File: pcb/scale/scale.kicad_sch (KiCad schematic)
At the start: 86 parts, among them J1 USB_C_Receptacle_USB2.0, J2 Conn_01x07, J3 Conn_01x04, SW1 SW_Push, SW10 SW_Push, SW11 SW_Push, SW12 SW_Push, SW13 SW_Push, SW14 SW_Push, SW15 SW_Push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

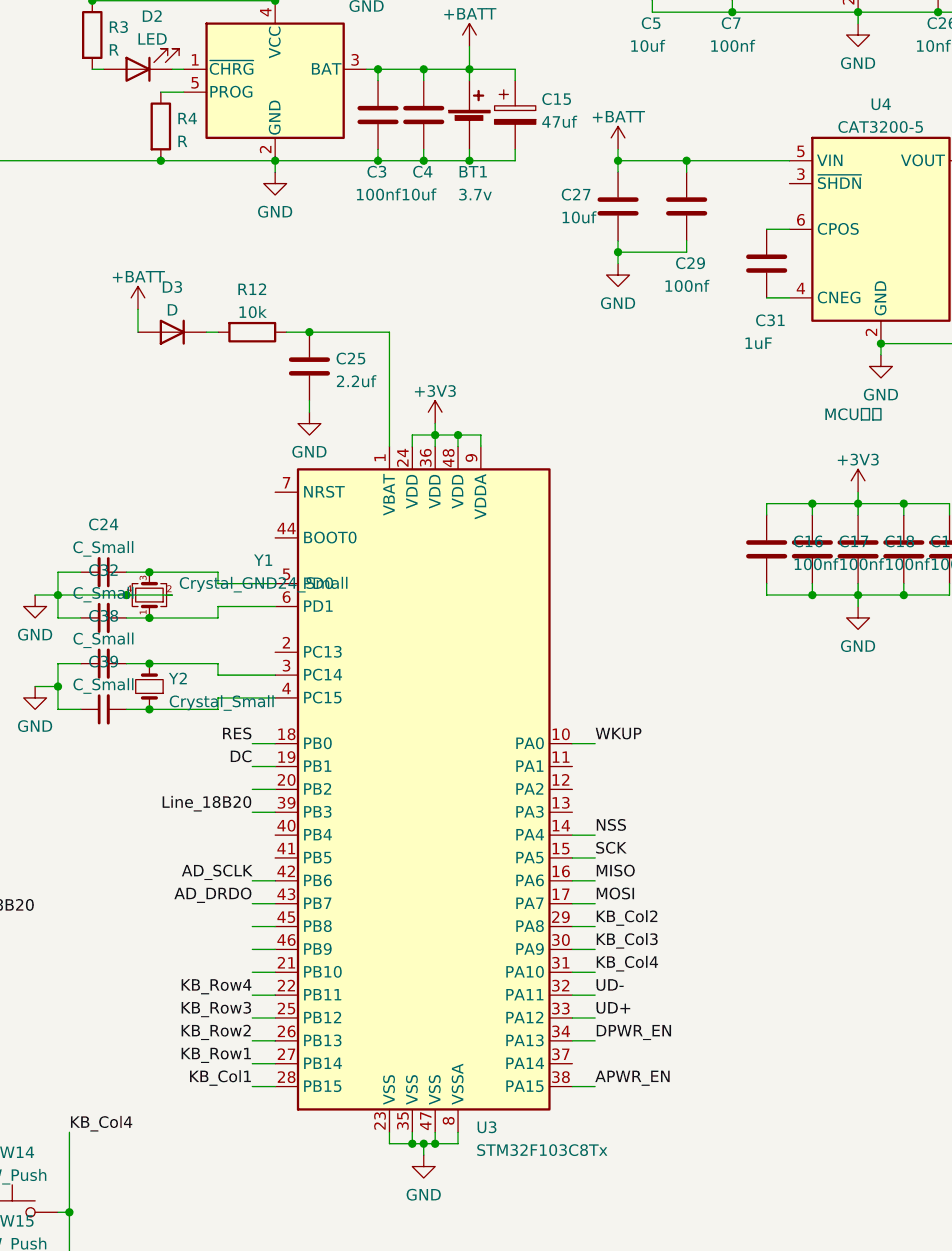
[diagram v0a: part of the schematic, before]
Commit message: 修复APWR_EN布线，ADC数字信号连接到其他引脚
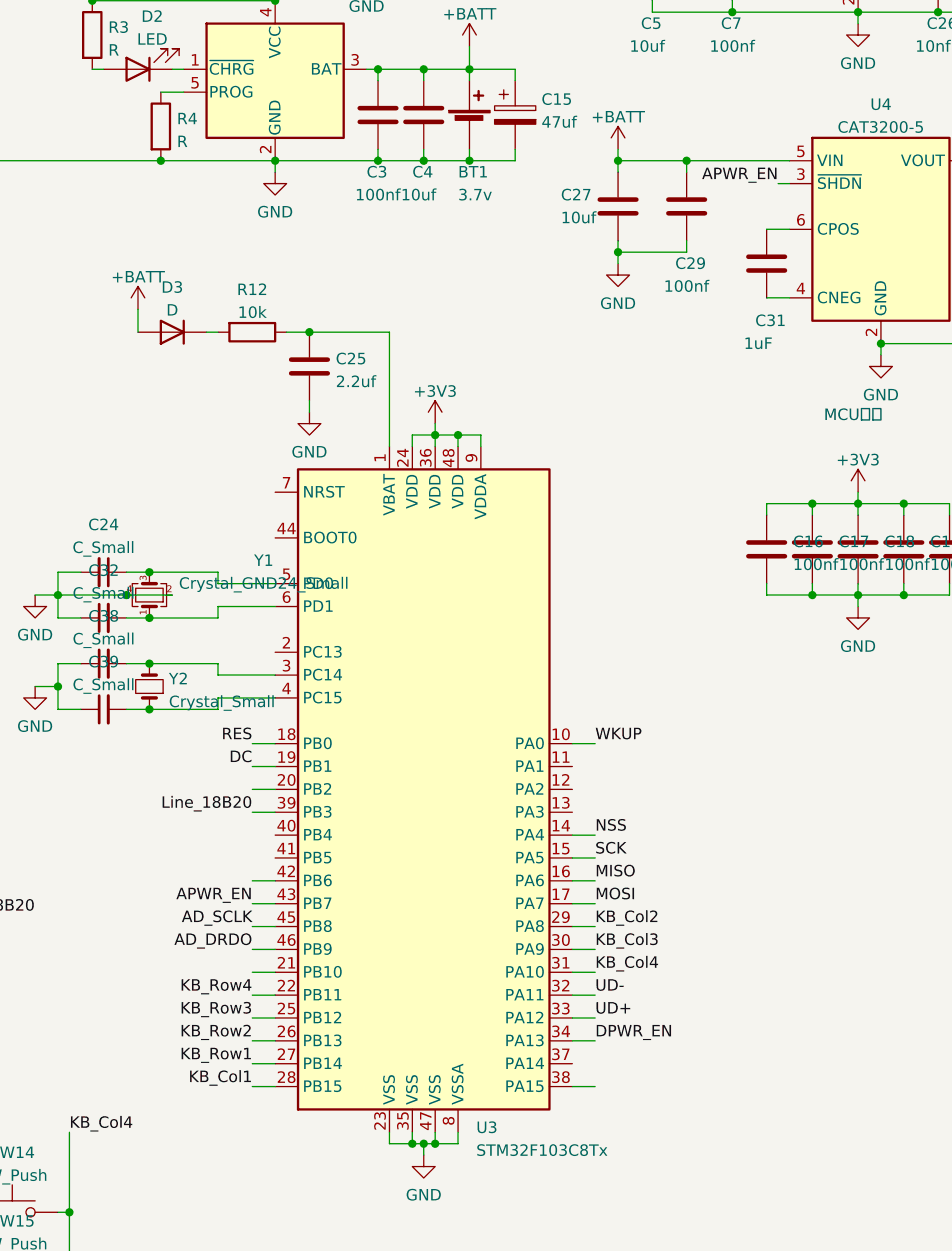
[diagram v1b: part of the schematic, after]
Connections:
- net AD_DRDO: now also U3.46 (PB9); no longer U3.43 (PB7)
- net AD_SCLK: now also U3.45 (PB8); no longer U3.42 (PB6)
- net APWR_EN: now also U3.43 (PB7), U4.3 (~{SHDN}); no longer U3.38 (PA15)
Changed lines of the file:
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@@
+    (stroke (width 0) (type default) (color 0 0 0 0))
+  )
+  (wire (pts (xy 161.29 54.61) (xy 162.56 54.61))
     (stroke (width 0) (type default) (color 0 0 0 0))
   )
@@
     (effects (font (size 1.27 1.27)) (justify left bottom))
   )
+  (label "AD_SCLK" (at 102.87 137.16 180)
+    (effects (font (size 1.27 1.27)) (justify right bottom))
+  )
   (label "MOSI" (at 229.87 83.82 0)
     (effects (font (size 1.27 1.27)) (justify left bottom))
@@
   (label "UD-" (at 64.77 29.21 0)
     (effects (font (size 1.27 1.27)) (justify left bottom))
-  )
-  (label "AD_SCLK" (at 102.87 132.08 180)
-    (effects (font (size 1.27 1.27)) (justify right bottom))
   )
   (label "KB_Row2" (at 102.87 149.86 180)
@@
     (effects (font (size 1.27 1.27)) (justify left bottom))
   )
+  (label "AD_DRDO" (at 102.87 139.7 180)
+    (effects (font (size 1.27 1.27)) (justify right bottom))
+  )
   (label "KB_Row4" (at 102.87 144.78 180)
     (effects (font (size 1.27 1.27)) (justify right bottom))
@@
   (label "DC" (at 229.87 88.9 0)
     (effects (font (size 1.27 1.27)) (justify left bottom))
-  )
-  (label "AD_DRDO" (at 102.87 134.62 180)
-    (effects (font (size 1.27 1.27)) (justify right bottom))
   )
   (label "KB_Col3" (at 67.31 160.02 0)
@@
     (effects (font (size 1.27 1.27)) (justify left bottom))
   )
+  (label "APWR_EN" (at 161.29 54.61 180)
+    (effects (font (size 1.27 1.27)) (justify right bottom))
+  )
   (label "NSS" (at 229.87 91.44 0)
-    (effects (font (size 1.27 1.27)) (justify left bottom))
-  )
-  (label "APWR_EN" (at 140.97 154.94 0)
     (effects (font (size 1.27 1.27)) (justify left bottom))
   )
@@
     (effects (font (size 1.27 1.27)) (justify right bottom))
   )
+  (label "APWR_EN" (at 102.87 134.62 180)
+    (effects (font (size 1.27 1.27)) (justify right bottom))
+  )

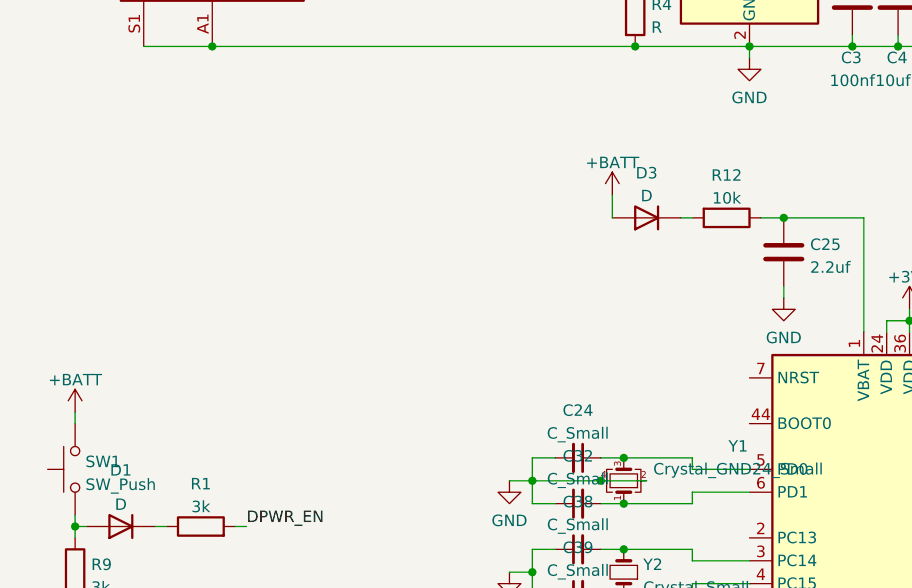
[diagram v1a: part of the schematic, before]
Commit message: 移除0402元件位号，添加NRST和BOOT0电路
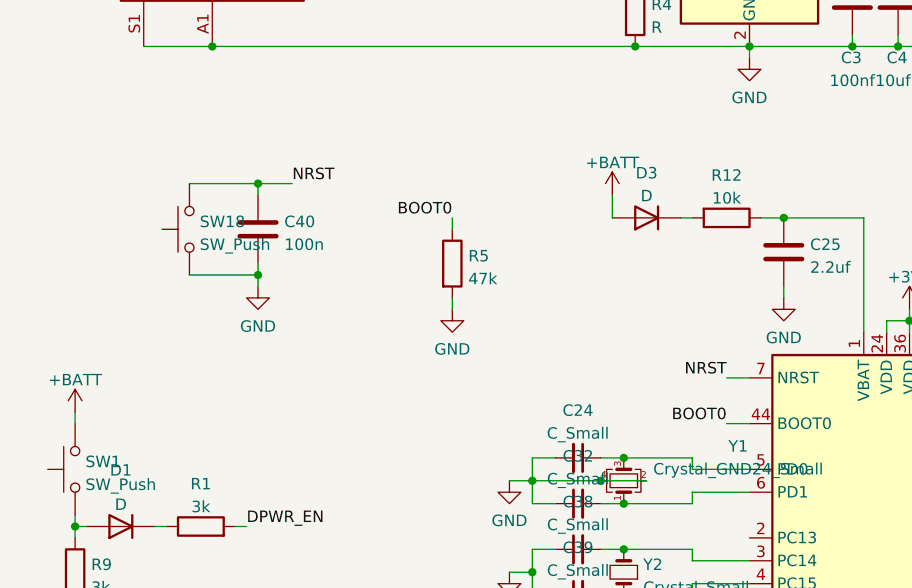
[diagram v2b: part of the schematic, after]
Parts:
- added C40: 100n, Capacitor_SMD:C_0603_1608Metric, symbol Device:C
- added R5: 47k, Resistor_SMD:R_0402_1005Metric, symbol Device:R
- added SW18: SW_Push, Button_Switch_SMD:SW_Push_SPST_NO_Alps_SKRK, symbol Switch:SW_Push
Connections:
- net GND: now also C40.2, R5.2, SW18.1
- net BOOT0: now reaches U3.44 (BOOT0)
- net BOOT0: now also R5.1
- net NRST: now reaches U3.7 (NRST)
- net NRST: now also C40.1, SW18.2
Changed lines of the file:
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@@
   (junction (at 88.9 100.33) (diameter 0) (color 0 0 0 0)
   )
+  (junction (at 50.8 77.47) (diameter 0) (color 0 0 0 0)
+  )
   (junction (at 156.21 35.56) (diameter 0) (color 0 0 0 0)
   )
@@
   (junction (at 30.48 115.57) (diameter 0) (color 0 0 0 0)
   )
+  (junction (at 50.8 67.31) (diameter 0) (color 0 0 0 0)
+  )
   (junction (at 25.4 193.04) (diameter 0) (color 0 0 0 0)
   )
@@
     (stroke (width 0) (type default) (color 0 0 0 0))
   )
+  (wire (pts (xy 50.8 67.31) (xy 50.8 68.58))
+    (stroke (width 0) (type default) (color 0 0 0 0))
+  )
   (wire (pts (xy 194.31 60.96) (xy 194.31 62.23))
     (stroke (width 0) (type default) (color 0 0 0 0))
@@
     (stroke (width 0) (type default) (color 0 0 0 0))
   )
+  (wire (pts (xy 105.41 93.98) (xy 102.87 93.98))
+    (stroke (width 0) (type default) (color 0 0 0 0))
+  )
   (wire (pts (xy 172.72 72.39) (xy 184.15 72.39))
     (stroke (width 0) (type default) (color 0 0 0 0))
@@
     (stroke (width 0) (type default) (color 0 0 0 0))
   )
+  (wire (pts (xy 43.18 67.31) (xy 50.8 67.31))
+    (stroke (width 0) (type default) (color 0 0 0 0))
+  )
   (wire (pts (xy 40.64 168.91) (xy 40.64 170.18))
     (stroke (width 0) (type default) (color 0 0 0 0))
@@
     (stroke (width 0) (type default) (color 0 0 0 0))
   )
+  (wire (pts (xy 50.8 78.74) (xy 50.8 77.47))
+    (stroke (width 0) (type default) (color 0 0 0 0))
+  )
   (wire (pts (xy 175.26 91.44) (xy 175.26 90.17))
     (stroke (width 0) (type default) (color 0 0 0 0))
@@
     (stroke (width 0) (type default) (color 0 0 0 0))
   )
+  (wire (pts (xy 50.8 77.47) (xy 50.8 76.2))
+    (stroke (width 0) (type default) (color 0 0 0 0))
+  )
   (wire (pts (xy 99.06 99.06) (xy 99.06 97.79))
     (stroke (width 0) (type default) (color 0 0 0 0))
@@
     (stroke (width 0) (type default) (color 0 0 0 0))
   )
+  (wire (pts (xy 102.87 88.9) (xy 105.41 88.9))
+    (stroke (width 0) (type default) (color 0 0 0 0))
+  )
   (wire (pts (xy 140.97 116.84) (xy 138.43 116.84))
     (stroke (width 0) (type default) (color 0 0 0 0))
@@
     (stroke (width 0) (type default) (color 0 0 0 0))
   )
+  (wire (pts (xy 43.18 77.47) (xy 50.8 77.47))
+    (stroke (width 0) (type default) (color 0 0 0 0))
+  )
   (wire (pts (xy 106.68 27.94) (xy 105.41 27.94))
     (stroke (width 0) (type default) (color 0 0 0 0))
@@
     (stroke (width 0) (type default) (color 0 0 0 0))
   )
+  (wire (pts (xy 72.39 72.39) (xy 72.39 71.12))
+    (stroke (width 0) (type default) (color 0 0 0 0))
+  )
   (wire (pts (xy 102.87 142.24) (xy 105.41 142.24))
     (stroke (width 0) (type default) (color 0 0 0 0))
@@
     (stroke (width 0) (type default) (color 0 0 0 0))
   )
+  (wire (pts (xy 50.8 67.31) (xy 54.61 67.31))
+    (stroke (width 0) (type default) (color 0 0 0 0))
+  )
   (wire (pts (xy 90.17 71.12) (xy 90.17 68.58))
     (stroke (width 0) (type default) (color 0 0 0 0))
@@
     (stroke (width 0) (type default) (color 0 0 0 0))
   )
+  (wire (pts (xy 72.39 80.01) (xy 72.39 81.28))
+    (stroke (width 0) (type default) (color 0 0 0 0))
+  )
   (wire (pts (xy 81.28 97.79) (xy 81.28 100.33))
     (stroke (width 0) (type default) (color 0 0 0 0))
@@
     (effects (font (size 1.27 1.27)) (justify left bottom))
   )
+  (label "BOOT0" (at 72.39 71.12 180)
+    (effects (font (size 1.27 1.27)) (justify right bottom))
+  )
   (label "KB_Col3" (at 140.97 139.7 0)
     (effects (font (size 1.27 1.27)) (justify left bottom))
@@
     (effects (font (size 1.27 1.27)) (justify right bottom))
   )
+  (label "NRST" (at 102.87 88.9 180)
+    (effects (font (size 1.27 1.27)) (justify right bottom))
+  )
   (label "KB_Col1" (at 102.87 154.94 180)
     (effects (font (size 1.27 1.27)) (justify right bottom))
@@
     (effects (font (size 1.27 1.27)) (justify right bottom))
   )
+  (label "BOOT0" (at 102.87 93.98 180)
+    (effects (font (size 1.27 1.27)) (justify right bottom))
+  )
   (label "DC" (at 229.87 88.9 0)
     (effects (font (size 1.27 1.27)) (justify left bottom))
   )
+  (label "NRST" (at 54.61 67.31 0)
+    (effects (font (size 1.27 1.27)) (justify left bottom))
+  )
   (label "KB_Col3" (at 67.31 160.02 0)
     (effects (font (size 1.27 1.27)) (justify left bottom))
@@
     (pin "2")
   )
+  (symbol (lib_id "Device:C") (at 50.8 72.39 0) (unit 1)
+    (in_bom yes) (on_board yes) (fields_autoplaced)
+    (property "Reference" "C40" (id 0) (at 53.721 71.5553 0)
+      (effects (font (size 1.27 1.27)) (justify left))
+    )
+    (property "Value" "100n" (id 1) (at 53.721 74.0922 0)
+      (effects (font (size 1.27 1.27)) (justify left))
+    )
+    (property "Footprint" "Capacitor_SMD:C_0603_1608Metric" (id 2) (at 51.7652 76.2 0)
+      (effects (font (size 1.27 1.27)) hide)
+    )
+    (property "Datasheet" "~" (id 3) (at 50.8 72.39 0)
+      (effects (font (size 1.27 1.27)) hide)
+    )
+    (pin "1")
+    (pin "2")
+  )
   (symbol (lib_id "power:GND") (at 255.27 83.82 0) (unit 1)
     (in_bom yes) (on_board yes) (fields_autoplaced)
@@
     (pin "1")
   )
+  (symbol (lib_id "power:GND") (at 72.39 81.28 0) (unit 1)
+    (in_bom yes) (on_board yes) (fields_autoplaced)
+    (property "Reference" "#PWR012" (id 0) (at 72.39 87.63 0)
+      (effects (font (size 1.27 1.27)) hide)
+    )
+    (property "Value" "GND" (id 1) (at 72.39 85.7234 0))
+    (property "Footprint" "" (id 2) (at 72.39 81.28 0)
+      (effects (font (size 1.27 1.27)) hide)
+    )
+    (property "Datasheet" "" (id 3) (at 72.39 81.28 0)
+      (effects (font (size 1.27 1.27)) hide)
+    )
+    (pin "1")
+  )
   (symbol (lib_id "Device:Battery_Cell") (at 127 48.26 0) (unit 1)
     (in_bom yes) (on_board yes)
@@
     (pin "1")
   )
+  (symbol (lib_id "Device:R") (at 72.39 76.2 0) (unit 1)
+    (in_bom yes) (on_board yes) (fields_autoplaced)
+    (property "Reference" "R5" (id 0) (at 74.168 75.3653 0)
+      (effects (font (size 1.27 1.27)) (justify left))
+    )
+    (property "Value" "47k" (id 1) (at 74.168 77.9022 0)
+      (effects (font (size 1.27 1.27)) (justify left))
+    )
+    (property "Footprint" "Resistor_SMD:R_0402_1005Metric" (id 2) (at 70.612 76.2 90)
+      (effects (font (size 1.27 1.27)) hide)
+    )
+    (property "Datasheet" "~" (id 3) (at 72.39 76.2 0)
+      (effects (font (size 1.27 1.27)) hide)
+    )
+    (pin "1")
+    (pin "2")
+  )
   (symbol (lib_id "Device:C") (at 189.23 57.15 0) (unit 1)
     (in_bom yes) (on_board yes)
@@
     (pin "2")
   )
+  (symbol (lib_id "Switch:SW_Push") (at 43.18 72.39 90) (unit 1)
+    (in_bom yes) (on_board yes) (fields_autoplaced)
+    (property "Reference" "SW18" (id 0) (at 44.323 71.5553 90)
+      (effects (font (size 1.27 1.27)) (justify right))
+    )
+    (property "Value" "SW_Push" (id 1) (at 44.323 74.0922 90)
+      (effects (font (size 1.27 1.27)) (justify right))
+    )
+    (property "Footprint" "Button_Switch_SMD:SW_Push_SPST_NO_Alps_SKRK" (id 2) (at 38.1 72.39 0)
+      (effects (font (size 1.27 1.27)) hide)
+    )
+    (property "Datasheet" "~" (id 3) (at 38.1 72.39 0)
+      (effects (font (size 1.27 1.27)) hide)
+    )
+    (pin "1")
+    (pin "2")
+  )
   (symbol (lib_id "Device:C_Small") (at 86.36 107.95 90) (unit 1)
     (in_bom yes) (on_board yes) (fields_autoplaced)
@@
     (pin "2")
   )
+  (symbol (lib_id "power:GND") (at 50.8 78.74 0) (unit 1)
+    (in_bom yes) (on_board yes) (fields_autoplaced)
+    (property "Reference" "#PWR01" (id 0) (at 50.8 85.09 0)
+      (effects (font (size 1.27 1.27)) hide)
+    )
+    (property "Value" "GND" (id 1) (at 50.8 83.1834 0))
+    (property "Footprint" "" (id 2) (at 50.8 78.74 0)
+      (effects (font (size 1.27 1.27)) hide)
+    )
+    (property "Datasheet" "" (id 3) (at 50.8 78.74 0)
+      (effects (font (size 1.27 1.27)) hide)
+    )
+    (pin "1")
+  )
   (sheet_instances
     (path "/" (page "1"))
   )
   (symbol_instances
+    (path "/fe68bfb8-996e-4576-9b8d-550a3d72da11"
+      (reference "#PWR01") (unit 1) (value "GND") (footprint "")
+    )
     (path "/8aca9b0c-d4ec-4cd3-81a7-caf98d8f1847"
       (reference "#PWR02") (unit 1) (value "+BATT") (footprint "")
@@
       (reference "#PWR011") (unit 1) (value "GND") (footprint "")
     )
+    (path "/32b72261-bee1-4ebc-a821-49a978820a9e"
+      (reference "#PWR012") (unit 1) (value "GND") (footprint "")
+    )
     (path "/47df3208-78df-439e-9fa8-87ed8cce3db5"
       (reference "#PWR013") (unit 1) (value "GNDA") (footprint "")
@@
       (reference "C39") (unit 1) (value "C_Small") (footprint "Capacitor_SMD:C_0402_1005Metric")
     )
+    (path "/2cc894df-58a7-4856-95b3-e83086f33f9b"
+      (reference "C40") (unit 1) (value "100n") (footprint "Capacitor_SMD:C_0603_1608Metric")
+    )
     (path "/95ff0230-3af0-4a2c-9f11-7ba31d4ab2d3"
       (reference "C41") (unit 1) (value "100nf") (footprint "Capacitor_SMD:C_0603_1608Metric")
@@
       (reference "R4") (unit 1) (value "R") (footprint "Resistor_SMD:R_0603_1608Metric")
     )
+    (path "/501cb121-610e-4bc4-897e-69026f2e81bd"
+      (reference "R5") (unit 1) (value "47k") (footprint "Resistor_SMD:R_0402_1005Metric")
+    )
     (path "/8528590c-4fde-4930-bdc8-69921bfc6c8e"
       (reference "R6") (unit 1) (value "100") (footprint "Resistor_SMD:R_0402_1005Metric")
@@
       (reference "SW17") (unit 1) (value "SW_Push") (footprint "Button_Switch_SMD:SW_Push_SPST_NO_Alps_SKRK")
     )
+    (path "/b6646a48-9152-40f0-aa29-ebdafa1d9c66"
+      (reference "SW18") (unit 1) (value "SW_Push") (footprint "Button_Switch_SMD:SW_Push_SPST_NO_Alps_SKRK")
+    )
     (path "/479234cc-9281-45b4-a44f-679ed793bd61"
